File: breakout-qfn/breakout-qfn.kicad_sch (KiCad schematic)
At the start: 42 parts, among them J1 Conn_01x04, U1 Openframe_QFN_TT06_REV2, U2 24LC02

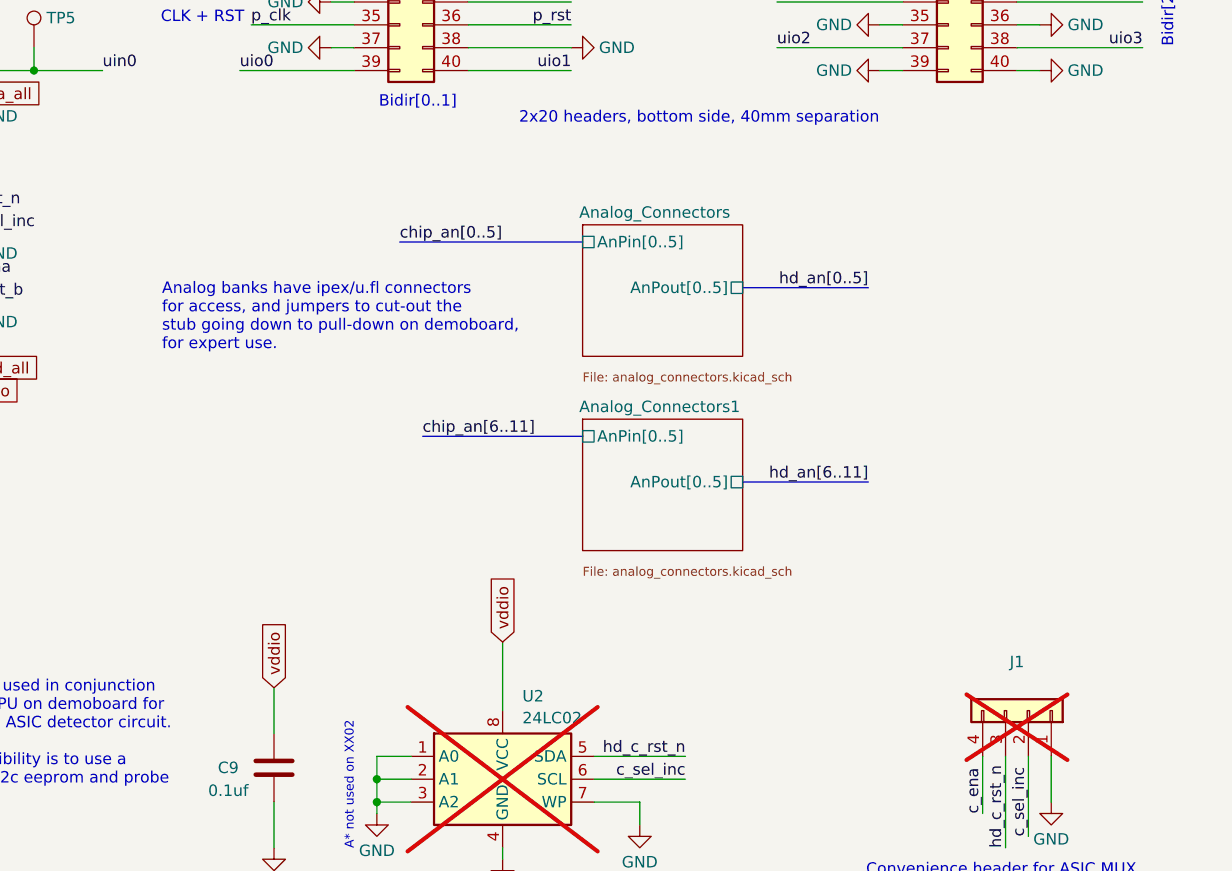
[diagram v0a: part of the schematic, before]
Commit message: TT08 breakout and documentation refactor
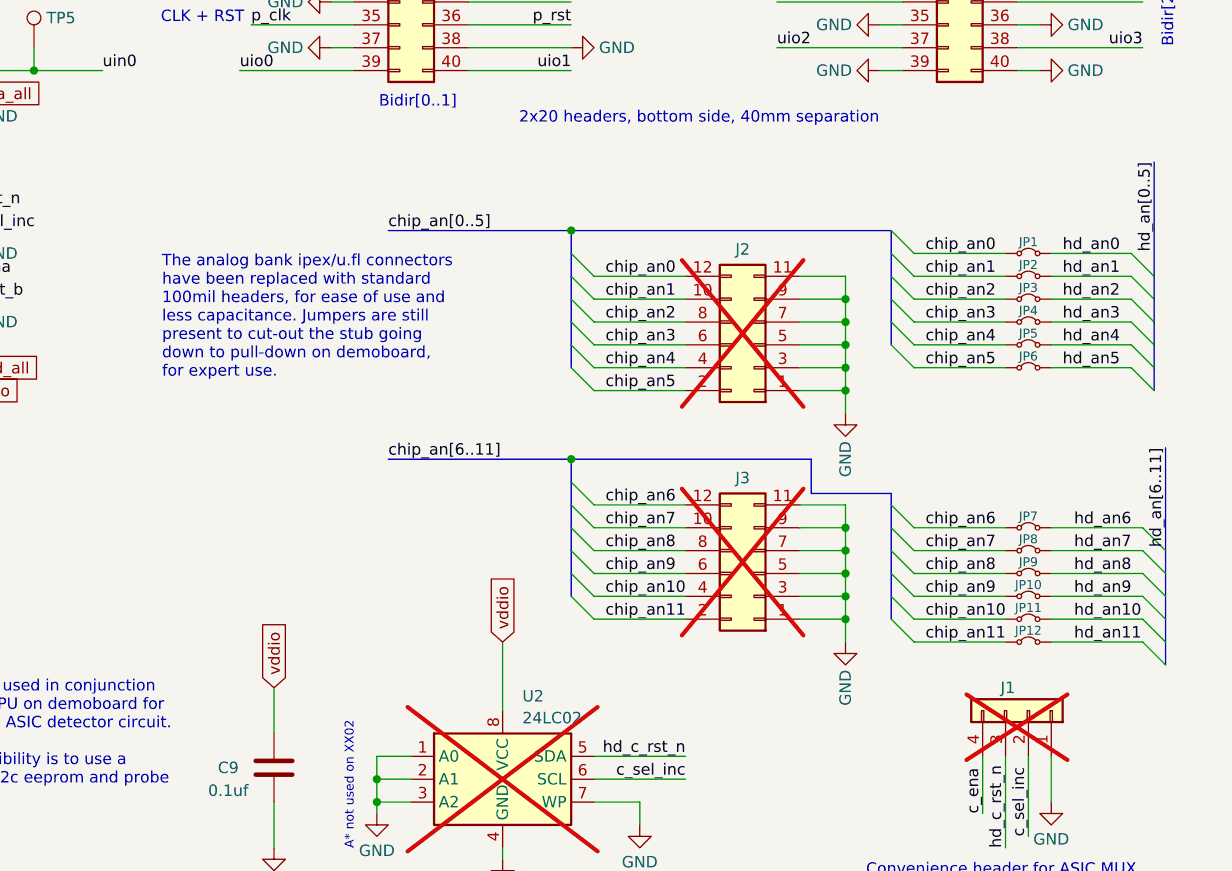
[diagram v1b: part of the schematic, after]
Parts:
- added J2, J3: Conn_02x06_Odd_Even, Connector_PinHeader_2.54mm:PinHeader_2x06_P2.54mm_Vertical, symbol Connector_Generic:Conn_02x06_Odd_Even
- added JP1, JP10, JP11, JP12, JP2, JP3, JP4, JP5, JP6, JP7, JP8, JP9: Jumper_2_Small_Bridged, TinyTapeout:SolderJumper-2_P1.3mm_Bridged_RoundedPad1.0x1.5mmEasyCut, symbol Jumper:Jumper_2_Small_Bridged
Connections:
- net GND: now also J2.1 (Pin_1), J2.11 (Pin_11), J2.3 (Pin_3), J2.5 (Pin_5), J2.7 (Pin_7), J2.9 (Pin_9), J3.1 (Pin_1), J3.11 (Pin_11), J3.3 (Pin_3), J3.5 (Pin_5), J3.7 (Pin_7), J3.9 (Pin_9)
- net chip_an0: now also J2.12 (Pin_12), JP1.1 (A)
- net chip_an1: now also J2.10 (Pin_10), JP2.1 (A)
- net chip_an10: now also J3.4 (Pin_4), JP11.1 (A)
- net chip_an11: now also J3.2 (Pin_2), JP12.1 (A)
- net chip_an2: now also J2.8 (Pin_8), JP3.1 (A)
- net chip_an3: now also J2.6 (Pin_6), JP4.1 (A)
- net chip_an4: now also J2.4 (Pin_4), JP5.1 (A)
- net chip_an5: now also J2.2 (Pin_2), JP6.1 (A)
- net chip_an6: now also J3.12 (Pin_12), JP7.1 (A)
- net chip_an7: now also J3.10 (Pin_10), JP8.1 (A)
- net chip_an8: now also J3.8 (Pin_8), JP9.1 (A)
- net chip_an9: now also J3.6 (Pin_6), JP10.1 (A)
- net hd_an0: now also JP1.2 (B)
- net hd_an1: now also JP2.2 (B)
- net hd_an10: now also JP11.2 (B)
- net hd_an11: now also JP12.2 (B)
- net hd_an2: now also JP3.2 (B)
- net hd_an3: now also JP4.2 (B)
- net hd_an4: now also JP5.2 (B)
- net hd_an5: now also JP6.2 (B)
- net hd_an6: now also JP7.2 (B)
- net hd_an7: now also JP8.2 (B)
- net hd_an8: now also JP9.2 (B)
- net hd_an9: now also JP10.2 (B)
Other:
- removed sheet Analog_Connectors
- removed sheet Analog_Connectors1
- note added: "The analog bank ipex/u.fl connectors have been replaced with standard 100mil headers, for ease of use and less capacitance. Jumpers are still present to cut-out the stub going down to pull-down on demoboard, for expert use."
- note removed: "Analog banks have ipex/u.fl connectors for access, and jumpers to cut-out the stub going down to pull-down on demoboard, for expert use."
- title: TT07 Openframe breakout -> TT08 Openframe breakout

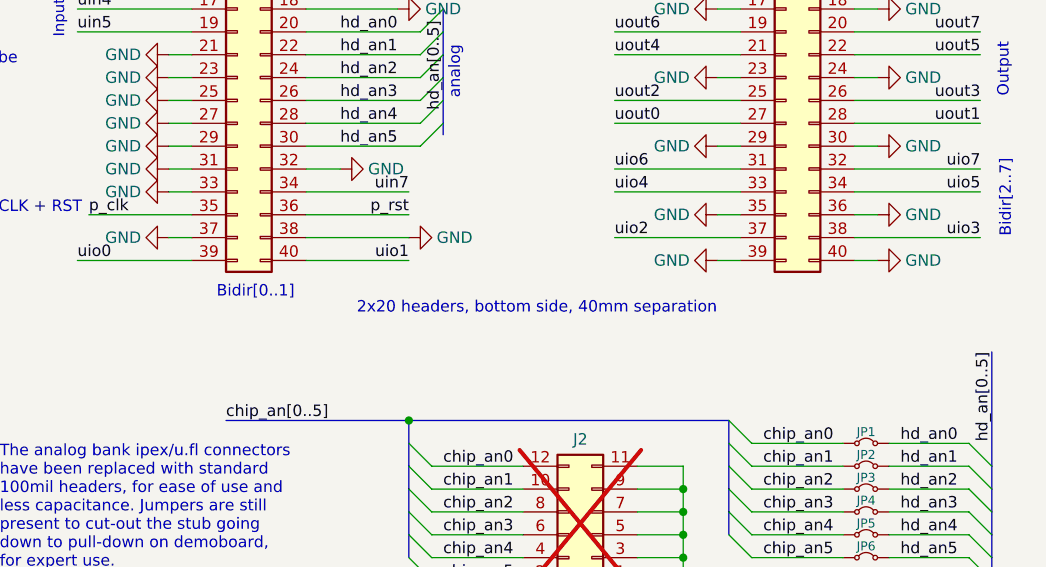
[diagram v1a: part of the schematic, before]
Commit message: Fab layer cleanup and BOM MPNs
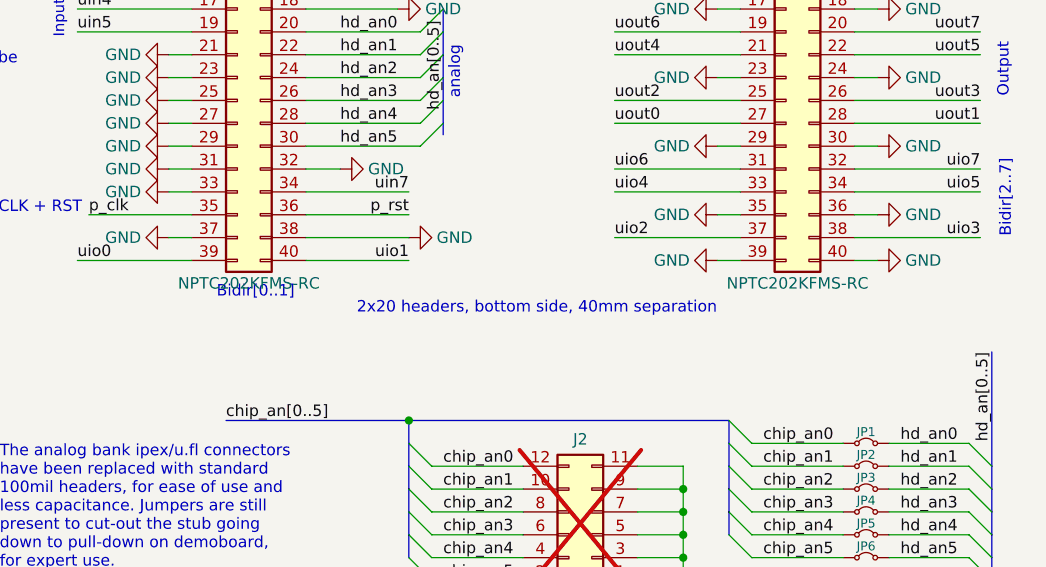
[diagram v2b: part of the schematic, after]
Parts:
- CON1, CON2: value ~ -> NPTC202KFMS-RC
- R3, R4: DigikeyPN (none) -> 13-RC1206FR-130RLCT-ND; LCSC (none) -> C137394; MPN (none) -> RC1206FR-130RL; MPN_ALT (none) -> WR12X000 PTL
- R6, R7: DigikeyPN (none) -> 311-0.0JRCT-ND; LCSC (none) -> C60485; MPN (none) -> RC0402JR-070RL; MPN_ALT (none) -> WR04X000 PTL
- U1: MPN (none) -> TT_ASIC
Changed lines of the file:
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@@
 			)
 		)
+		(property "MPN" "TT_ASIC"
+			(at 91.44 95.25 0)
+			(effects
+				(font
+					(size 1.27 1.27)
+				)
+				(hide yes)
+			)
+		)
 		(pin "41"
 		)
@@
 			)
 		)
-		(property "Value" "~"
+		(property "Value" "NPTC202KFMS-RC"
 			(at 180.34 78.74 0)
 			(effects
@@
 			)
 		)
-		(property "MPN" ""
+		(property "MPN" "RC0402JR-070RL"
 			(at 133.35 187.96 0)
 			(effects
@@
 			)
 		)
-		(property "MPN_ALT" ""
+		(property "MPN_ALT" "WR04X000 PTL"
 			(at 133.35 187.96 0)
 			(effects
@@
 			)
 		)
-		(property "DigikeyPN" ""
+		(property "DigikeyPN" "311-0.0JRCT-ND"
 			(at 133.35 187.96 0)
 			(effects
@@
 			)
 		)
+		(property "LCSC" "C60485"
+			(at 133.35 187.96 0)
+			(effects
+				(font
+					(size 1.27 1.27)
+				)
+				(hide yes)
+			)
+		)
 		(pin "2"
 		)
@@
 			)
 		)
-		(property "MPN" ""
+		(property "MPN" "RC1206FR-130RL"
 			(at 121.92 41.91 0)
 			(effects
@@
 			)
 		)
-		(property "MPN_ALT" ""
+		(property "MPN_ALT" "WR12X000 PTL"
 			(at 121.92 41.91 0)
 			(effects
@@
 			)
 		)
-		(property "DigikeyPN" ""
+		(property "DigikeyPN" "13-RC1206FR-130RLCT-ND"
 			(at 121.92 41.91 0)
 			(effects
@@
 			)
 		)
+		(property "LCSC" "C137394"
+			(at 121.92 41.91 0)
+			(effects
+				(font
+					(size 1.27 1.27)
+				)
+				(hide yes)
+			)
+		)
 		(pin "2"
 		)
@@
 			)
 		)
-		(property "MPN" ""
+		(property "MPN" "RC0402JR-070RL"
 			(at 133.35 195.58 0)
 			(effects
@@
 			)
 		)
-		(property "MPN_ALT" ""
+		(property "MPN_ALT" "WR04X000 PTL"
 			(at 133.35 195.58 0)
 			(effects
@@
 			)
 		)
-		(property "DigikeyPN" ""
+		(property "DigikeyPN" "311-0.0JRCT-ND"
 			(at 133.35 195.58 0)
 			(effects
@@
 			)
 		)
+		(property "LCSC" "C60485"
+			(at 133.35 195.58 0)
+			(effects
+				(font
+					(size 1.27 1.27)
+				)
+				(hide yes)
+			)
+		)
 		(pin "2"
 		)
@@
 			)
 		)
-		(property "MPN" ""
+		(property "MPN" "RC1206FR-130RL"
 			(at 135.89 41.91 0)
 			(effects
@@
 			)
 		)
-		(property "MPN_ALT" ""
+		(property "MPN_ALT" "WR12X000 PTL"
 			(at 135.89 41.91 0)
 			(effects
@@
 			)
 		)
-		(property "DigikeyPN" ""
+		(property "DigikeyPN" "13-RC1206FR-130RLCT-ND"
 			(at 135.89 41.91 0)
 			(effects
@@
 			)
 		)
+		(property "LCSC" "C137394"
+			(at 135.89 41.91 0)
+			(effects
+				(font
+					(size 1.27 1.27)
+				)
+				(hide yes)
+			)
+		)
 		(pin "2"
 		)
@@
 			)
 		)
-		(property "Value" "~"
+		(property "Value" "NPTC202KFMS-RC"
 			(at 241.3 78.74 0)
 			(effects
